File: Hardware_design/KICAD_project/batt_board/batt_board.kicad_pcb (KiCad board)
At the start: 2 copper layers, 50 x 50 mm, 53 parts, among them U1 TPS5430DDA, U2 AMS1117-3.3

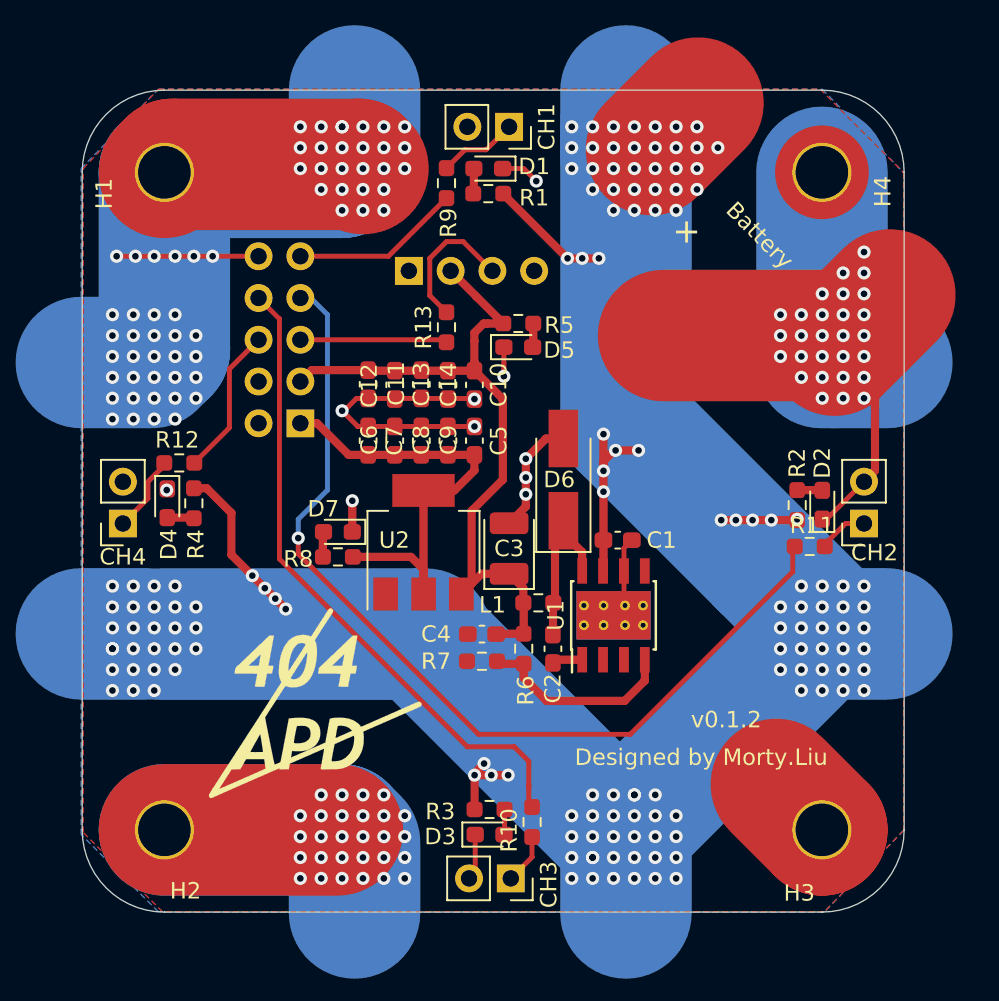
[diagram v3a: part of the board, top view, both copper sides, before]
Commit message: 控制系统硬件设计完成，电源板正式发布v1.0.0 控制板打样v0.2.0测试
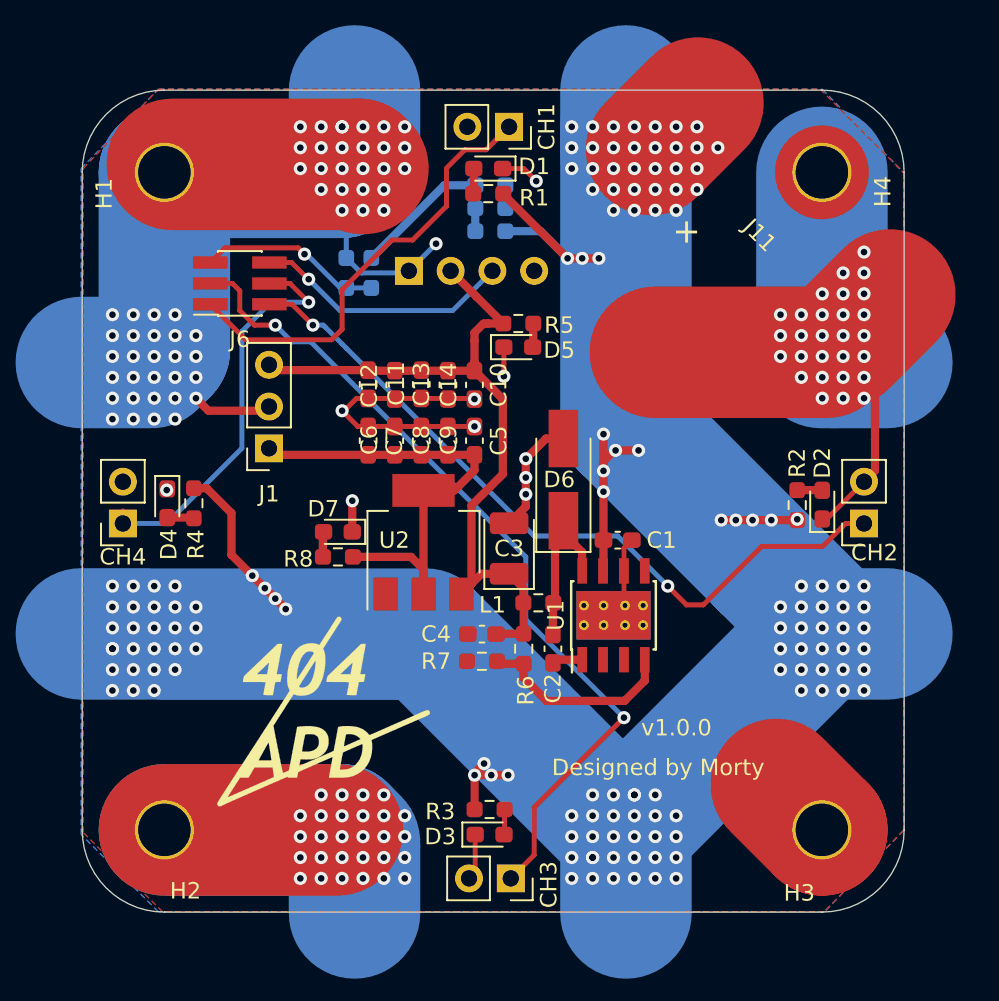
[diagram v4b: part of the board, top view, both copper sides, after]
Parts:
- removed conn2upper1: Conn_02x05_Counter_Clockwise, Connector_PinSocket_2.54mm:PinSocket_2x05_P2.54mm_Horizontal
- added J1: Conn_01x03, Connector_PinSocket_2.54mm:PinSocket_1x03_P2.54mm_Vertical, F.Cu at (126.4, 81.8)
- added J6: Conn_02x03_Counter_Clockwise, Connector_PinSocket_1.27mm:PinSocket_2x03_P1.27mm_Vertical_SMD, F.Cu at (124.6, 71.8)
- R10, R11, R12, R13, R9: value 22 -> 10k; moved to B.Cu
- moved R10 34.8 mm to (132.6, 71.1)
- moved R11 29.3 mm to (139.8, 65.8), turned to 0 degrees
- moved R12 24.5 mm to (139.8, 67.2), turned to 180 degrees
- moved R9 8.18 mm to (131.1, 71.1)
- moved R13 6.42 mm to (139.8, 68.6), turned to 0 degrees
- moved G*** 0.72 mm to (129.5, 97.9)
- renumbered Battery to J11, ESC3 to J2, ESC1 to J3, ESC2 to J4, ESC4 to J5
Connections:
- R10 pad 1: PWM_CH3 -> /ADC_IN
- R11 pad 1: PWM_CH2 -> Net-(R10-Pad2)
- R12 pad 1: PWM_CH4 -> Net-(R11-Pad2)
- R13 pad 1: Net-(R13-Pad1) -> Net-(R12-Pad2)
- R13 pad 2: PPM -> /VCC_IN
- R9 pad 1: PWM_CH1 -> GND
- R9 pad 2: Net-(R9-Pad2) -> /ADC_IN
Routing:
- net Net-(R11-Pad2): track 57.6 -> 1.40 mm, vias 1 -> 0
- net PWM_CH3: track 2.93 -> 51.6 mm, vias 0 -> 2
- net PWM_CH2: track 3.10 -> 45.8 mm, vias 0 -> 2
- net Net-(R10-Pad2): track 39.9 -> 8.31 mm
- net PWM_CH1: track 4.85 -> 27.2 mm
- net PWM_CH4: track 4.86 -> 24.7 mm, vias 0 -> 1
- net /ADC_IN: track 0.00 -> 11.4 mm, vias 0 -> 1
- net Net-(R9-Pad2): track 10.4 -> 0.00 mm
- net Net-(R13-Pad1): track 9.13 -> 0.00 mm
- net GND: track 171.6 -> 179.4 mm, vias 126 -> 121
- net Net-(R12-Pad2): track 9.11 -> 1.40 mm
- net PPM: track 8.94 -> 15.6 mm, vias 0 -> 1
- net /VCC_IN: track 131.9 -> 136.4 mm
- net +5V: track 47.4 -> 49.2 mm
- net +3V3: track 28.5 -> 29.8 mm
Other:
- board text added: "Designed by Morty"
- board text added: "v1.0.0"
- board text removed: "Designed by Morty.Liu"
- board text removed: "v0.1.2"
